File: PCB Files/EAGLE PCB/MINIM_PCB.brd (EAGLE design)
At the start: 33.6 x 24.6 mm, 22 parts, among them IC1 4066D, IC2 OP-AMP

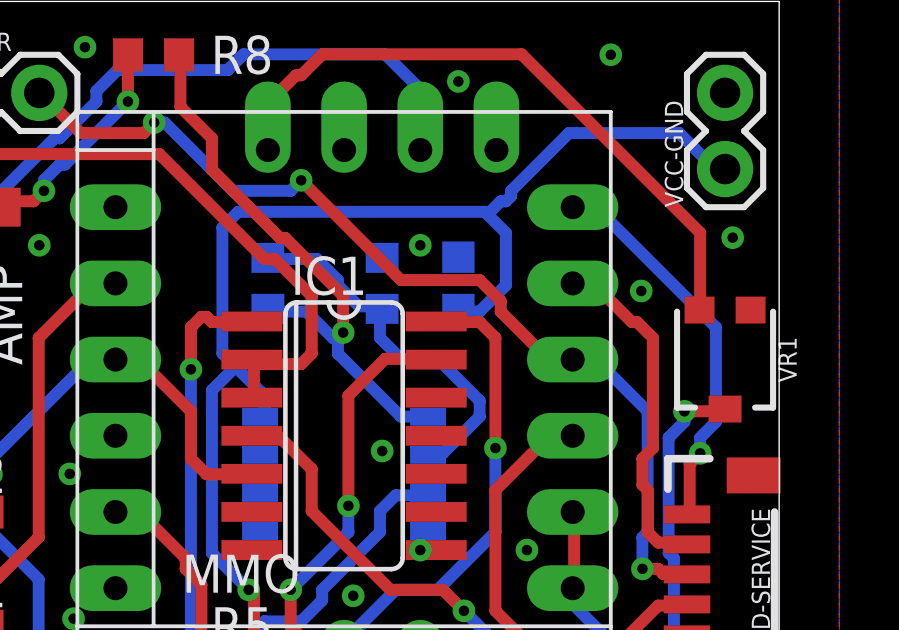
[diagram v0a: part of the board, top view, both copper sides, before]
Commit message: new pcb1 revision 3 (5v on RJ45 and OSD PCB footprint added)
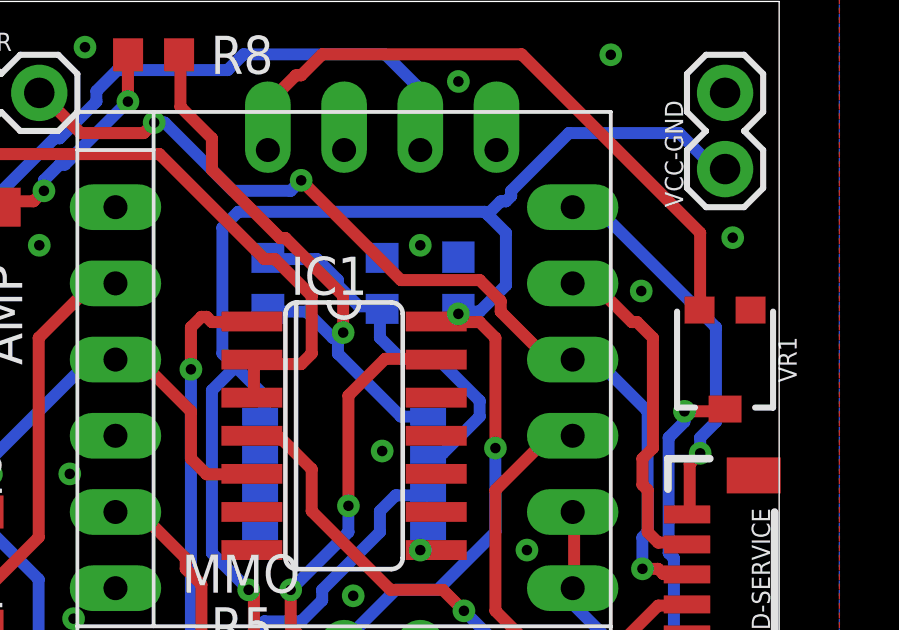
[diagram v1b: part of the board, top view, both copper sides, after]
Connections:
- net N$5 renamed VIDIN_AMP
- removed net VDD: IC1.14, MINIMOSD.IVCC
- net VCC: now also IC1.14, MINIMOSD.IVCC
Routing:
- net VCC: track 41.2 -> 58.7 mm, vias 1 -> 3
- net VDD: track 16.1 -> 0.00 mm, vias 1 -> 0
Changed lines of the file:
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@@
 <wire x1="43.05" y1="70" x2="43.18" y2="69.85" width="0.4" layer="16"/>
 <via x="27.3" y="55.825" extent="1-16" drill="0.35"/>
+<contactref element="IC1" pad="14"/>
+<contactref element="MINIMOSD" pad="IVCC"/>
+<wire x1="35" y1="64.75" x2="33.6" y2="64.75" width="0.4" layer="1"/>
+<wire x1="35.525" y1="64.225" x2="35" y2="64.75" width="0.4" layer="1"/>
+<wire x1="35.525" y1="60.55" x2="35.525" y2="64.225" width="0.4" layer="1"/>
+<wire x1="35.525" y1="57.75" x2="35.525" y2="60.55" width="0.4" layer="16"/>
+<wire x1="33.6" y1="55.825" x2="35.525" y2="57.75" width="0.4" layer="16"/>
+<wire x1="32.2" y1="55.825" x2="33.6" y2="55.825" width="0.4" layer="16"/>
+<wire x1="30.625" y1="54.25" x2="32.2" y2="55.825" width="0.4" layer="16"/>
+<wire x1="30.625" y1="53.375" x2="30.625" y2="54.25" width="0.4" layer="16"/>
+<wire x1="33.6" y1="64.75" x2="33.5534" y2="64.77" width="0.4" layer="1"/>
+<wire x1="30.625" y1="53.375" x2="30.48" y2="53.3" width="0.4" layer="16"/>
+<via x="35.525" y="60.55" extent="1-16" drill="0.35"/>
+<via x="34.29" y="65.024" extent="1-16" drill="0.35"/>
+<wire x1="34.29" y1="64.77" x2="34.29" y2="65.024" width="0.4" layer="1"/>
+<wire x1="34.29" y1="64.77" x2="33.5534" y2="64.77" width="0.4" layer="1"/>
+<wire x1="34.29" y1="64.77" x2="34.29" y2="65.024" width="0.4" layer="16"/>
+<wire x1="34.29" y1="65.024" x2="34.29" y2="65.165" width="0.4" layer="16"/>
 </signal>
 <signal name="VIDEO_IN">
@@
 <contactref element="IC1" pad="7"/>
 </signal>
-<signal name="VDD">
-<contactref element="IC1" pad="14"/>
-<contactref element="MINIMOSD" pad="IVCC"/>
-<wire x1="35" y1="64.75" x2="33.6" y2="64.75" width="0.4" layer="1"/>
-<wire x1="35.525" y1="64.225" x2="35" y2="64.75" width="0.4" layer="1"/>
-<wire x1="35.525" y1="60.55" x2="35.525" y2="64.225" width="0.4" layer="1"/>
-<wire x1="35.525" y1="57.75" x2="35.525" y2="60.55" width="0.4" layer="16"/>
-<wire x1="33.6" y1="55.825" x2="35.525" y2="57.75" width="0.4" layer="16"/>
-<wire x1="32.2" y1="55.825" x2="33.6" y2="55.825" width="0.4" layer="16"/>
-<wire x1="30.625" y1="54.25" x2="32.2" y2="55.825" width="0.4" layer="16"/>
-<wire x1="30.625" y1="53.375" x2="30.625" y2="54.25" width="0.4" layer="16"/>
-<wire x1="33.6" y1="64.75" x2="33.5534" y2="64.77" width="0.4" layer="1"/>
-<wire x1="30.625" y1="53.375" x2="30.48" y2="53.3" width="0.4" layer="16"/>
-<via x="35.525" y="60.55" extent="1-16" drill="0.35"/>
-</signal>
 <signal name="N$3">
 <contactref element="MINIMOSD" pad="BAT1"/>
@@
 <wire x1="28" y1="70.525" x2="27.94" y2="70.485" width="0.4" layer="1"/>
 </signal>
-<signal name="N$5">
+<signal name="VIDIN_AMP">
 <contactref element="R7" pad="1"/>
 <contactref element="IC2" pad="3"/>
